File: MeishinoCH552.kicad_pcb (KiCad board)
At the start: 2 copper layers, 91 x 55 mm, 20 parts, among them CN1 CON_USB-C-16, CN2 CON_USB-C-16, J1 Conn_01x06, J2 Conn_01x06, J3 Conn_01x08, J4 Conn_01x08, J5 USB_A, SW1 SW_Push, SW2 SW_Push, U1 MCU_CH552T

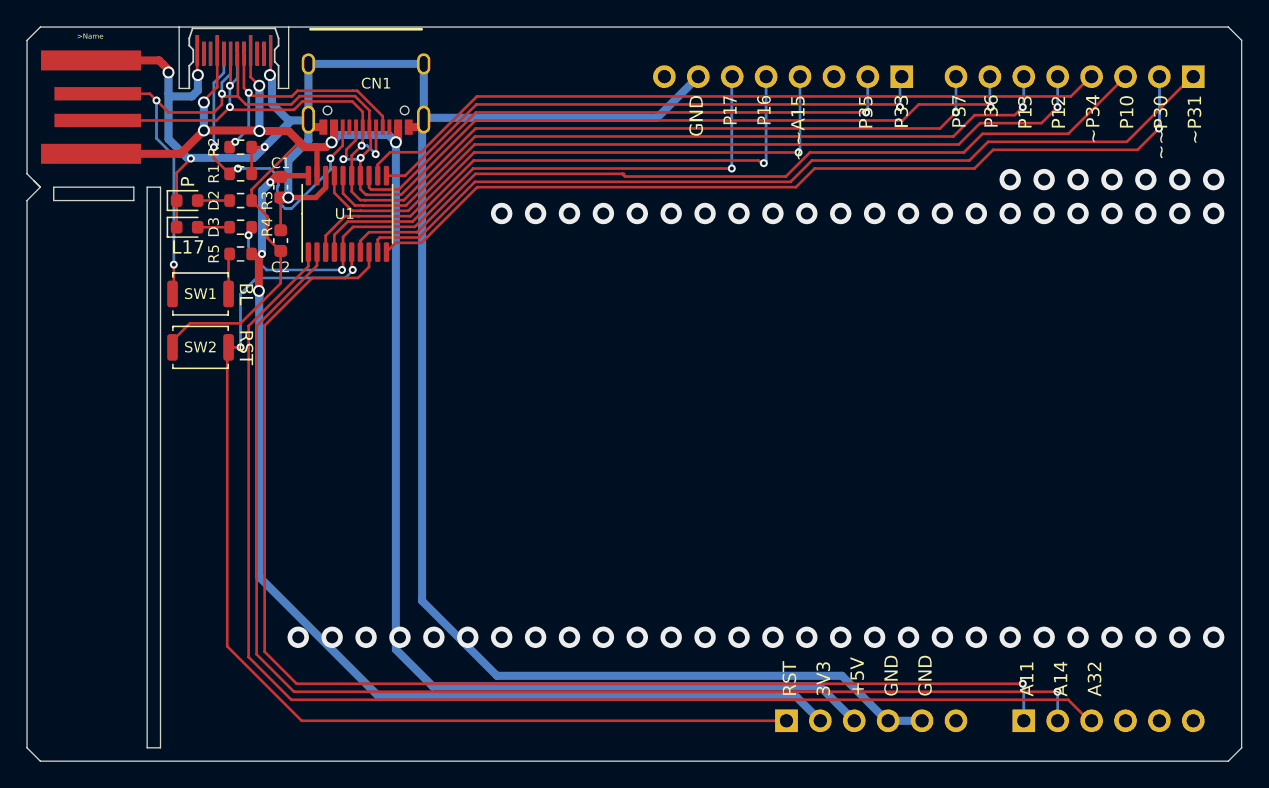
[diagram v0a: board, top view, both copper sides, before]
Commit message: フリー配線エリアのパッドをレジストなしに
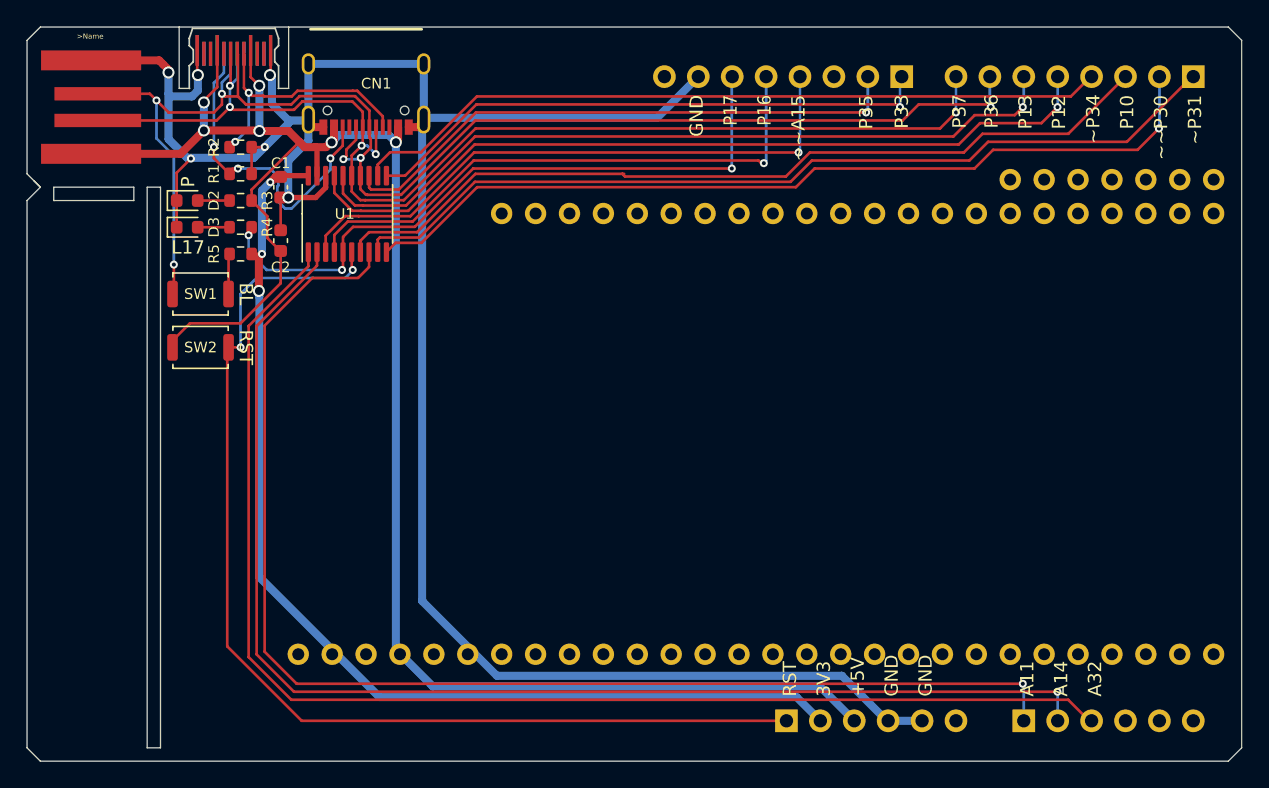
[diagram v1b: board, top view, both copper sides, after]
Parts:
- added REF**: Pad_TH09mm, akita:Pad_TH09mm, F.Cu at (68.6, 47.0)
- added REF**: Pad_TH09mm, akita:Pad_TH09mm, F.Cu at (53.3, 47.0)
- added REF**: Pad_TH09mm, akita:Pad_TH09mm, F.Cu at (73.7, 47.0)
- added REF**: Pad_TH09mm, akita:Pad_TH09mm, F.Cu at (83.8, 47.0)
- added REF**: Pad_TH09mm, akita:Pad_TH09mm, F.Cu at (43.2, 47.0)
- added REF**: Pad_TH09mm, akita:Pad_TH09mm, F.Cu at (48.3, 47.0)
- added REF**: Pad_TH09mm, akita:Pad_TH09mm, F.Cu at (66.0, 14.0)
- added REF**: Pad_TH09mm, akita:Pad_TH09mm, F.Cu at (50.8, 14.0)
- added REF**: Pad_TH09mm, akita:Pad_TH09mm, F.Cu at (27.9, 47.0)
- added REF**: Pad_TH09mm, akita:Pad_TH09mm, F.Cu at (63.5, 47.0)
- added REF**: Pad_TH09mm, akita:Pad_TH09mm, F.Cu at (33.0, 47.0)
- added REF**: Pad_TH09mm, akita:Pad_TH09mm, F.Cu at (83.8, 11.4)
- added REF**: Pad_TH09mm, akita:Pad_TH09mm, F.Cu at (61.0, 14.0)
- added REF**: Pad_TH09mm, akita:Pad_TH09mm, F.Cu at (20.3, 47.0)
- added REF**: Pad_TH09mm, akita:Pad_TH09mm, F.Cu at (86.4, 11.4)
- added REF**: Pad_TH09mm, akita:Pad_TH09mm, F.Cu at (81.3, 47.0)
- added REF**: Pad_TH09mm, akita:Pad_TH09mm, F.Cu at (81.3, 11.4)
- added REF**: Pad_TH09mm, akita:Pad_TH09mm, F.Cu at (48.3, 14.0)
- added REF**: Pad_TH09mm, akita:Pad_TH09mm, F.Cu at (61.0, 47.0)
- added REF**: Pad_TH09mm, akita:Pad_TH09mm, F.Cu at (50.8, 47.0)
- added REF**: Pad_TH09mm, akita:Pad_TH09mm, F.Cu at (88.9, 47.0)
- added REF**: Pad_TH09mm, akita:Pad_TH09mm, F.Cu at (88.9, 11.4)
- added REF**: Pad_TH09mm, akita:Pad_TH09mm, F.Cu at (55.9, 47.0)
- added REF**: Pad_TH09mm, akita:Pad_TH09mm, F.Cu at (71.1, 14.0)
- added REF**: Pad_TH09mm, akita:Pad_TH09mm, F.Cu at (53.3, 14.0)
- added REF**: Pad_TH09mm, akita:Pad_TH09mm, F.Cu at (83.8, 14.0)
- added REF**: Pad_TH09mm, akita:Pad_TH09mm, F.Cu at (40.6, 14.0)
- added REF**: Pad_TH09mm, akita:Pad_TH09mm, F.Cu at (40.6, 47.0)
- added REF**: Pad_TH09mm, akita:Pad_TH09mm, F.Cu at (30.5, 47.0)
- added REF**: Pad_TH09mm, akita:Pad_TH09mm, F.Cu at (63.5, 14.0)
- added REF**: Pad_TH09mm, akita:Pad_TH09mm, F.Cu at (78.7, 14.0)
- added REF**: Pad_TH09mm, akita:Pad_TH09mm, F.Cu at (25.4, 47.0)
- added REF**: Pad_TH09mm, akita:Pad_TH09mm, F.Cu at (76.2, 14.0)
- added REF**: Pad_TH09mm, akita:Pad_TH09mm, F.Cu at (68.6, 14.0)
- added REF**: Pad_TH09mm, akita:Pad_TH09mm, F.Cu at (88.9, 14.0)
- added REF**: Pad_TH09mm, akita:Pad_TH09mm, F.Cu at (73.7, 11.4)
- added REF**: Pad_TH09mm, akita:Pad_TH09mm, F.Cu at (86.4, 47.0)
- added REF**: Pad_TH09mm, akita:Pad_TH09mm, F.Cu at (81.3, 14.0)
- added REF**: Pad_TH09mm, akita:Pad_TH09mm, F.Cu at (58.4, 14.0)
- added REF**: Pad_TH09mm, akita:Pad_TH09mm, F.Cu at (35.6, 14.0)
- added REF**: Pad_TH09mm, akita:Pad_TH09mm, F.Cu at (71.1, 47.0)
- added REF**: Pad_TH09mm, akita:Pad_TH09mm, F.Cu at (43.2, 14.0)
- added REF**: Pad_TH09mm, akita:Pad_TH09mm, F.Cu at (45.7, 14.0)
- added REF**: Pad_TH09mm, akita:Pad_TH09mm, F.Cu at (38.1, 14.0)
- added REF**: Pad_TH09mm, akita:Pad_TH09mm, F.Cu at (78.7, 47.0)
- added REF**: Pad_TH09mm, akita:Pad_TH09mm, F.Cu at (78.7, 11.4)
- added REF**: Pad_TH09mm, akita:Pad_TH09mm, F.Cu at (76.2, 47.0)
- added REF**: Pad_TH09mm, akita:Pad_TH09mm, F.Cu at (45.7, 47.0)
- added REF**: Pad_TH09mm, akita:Pad_TH09mm, F.Cu at (66.0, 47.0)
- added REF**: Pad_TH09mm, akita:Pad_TH09mm, F.Cu at (73.7, 14.0)
- added REF**: Pad_TH09mm, akita:Pad_TH09mm, F.Cu at (38.1, 47.0)
- added REF**: Pad_TH09mm, akita:Pad_TH09mm, F.Cu at (22.9, 47.0)
- added REF**: Pad_TH09mm, akita:Pad_TH09mm, F.Cu at (55.9, 14.0)
- added REF**: Pad_TH09mm, akita:Pad_TH09mm, F.Cu at (35.6, 47.0)
- added REF**: Pad_TH09mm, akita:Pad_TH09mm, F.Cu at (76.2, 11.4)
- added REF**: Pad_TH09mm, akita:Pad_TH09mm, F.Cu at (58.4, 47.0)
- added REF**: Pad_TH09mm, akita:Pad_TH09mm, F.Cu at (86.4, 14.0)
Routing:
- net (no net): vias 57 -> 0
